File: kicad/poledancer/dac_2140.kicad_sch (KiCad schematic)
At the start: 19 parts, among them U7 AD5328

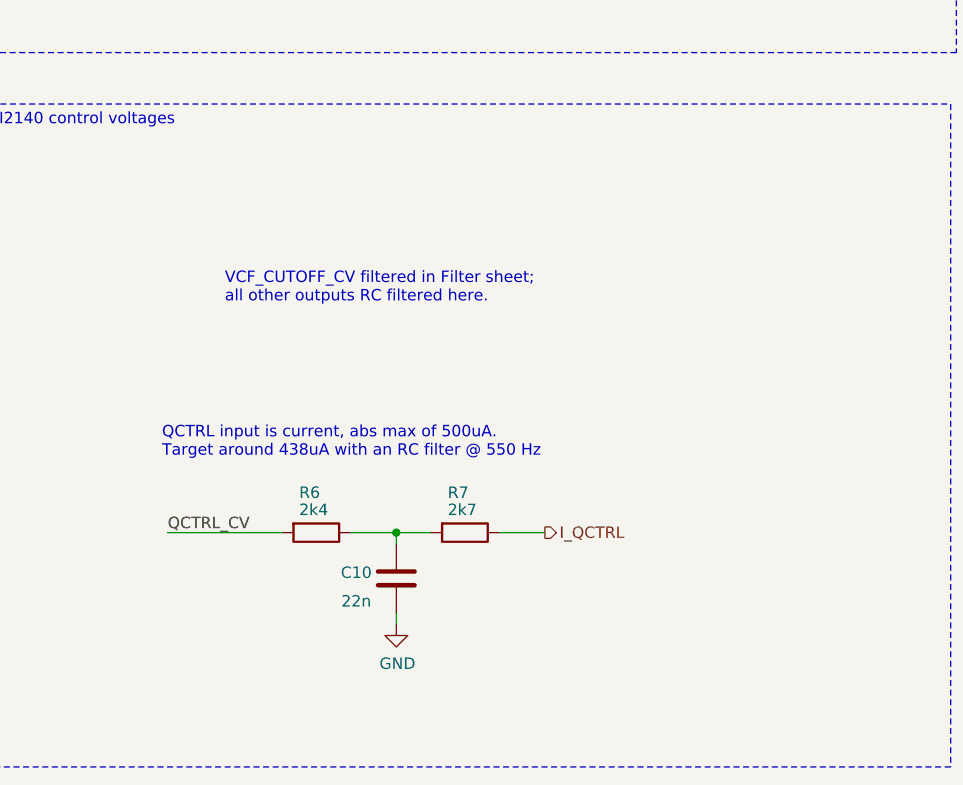
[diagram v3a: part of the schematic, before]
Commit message: create hand solder footprints for SSI chips.  Get some placement done.
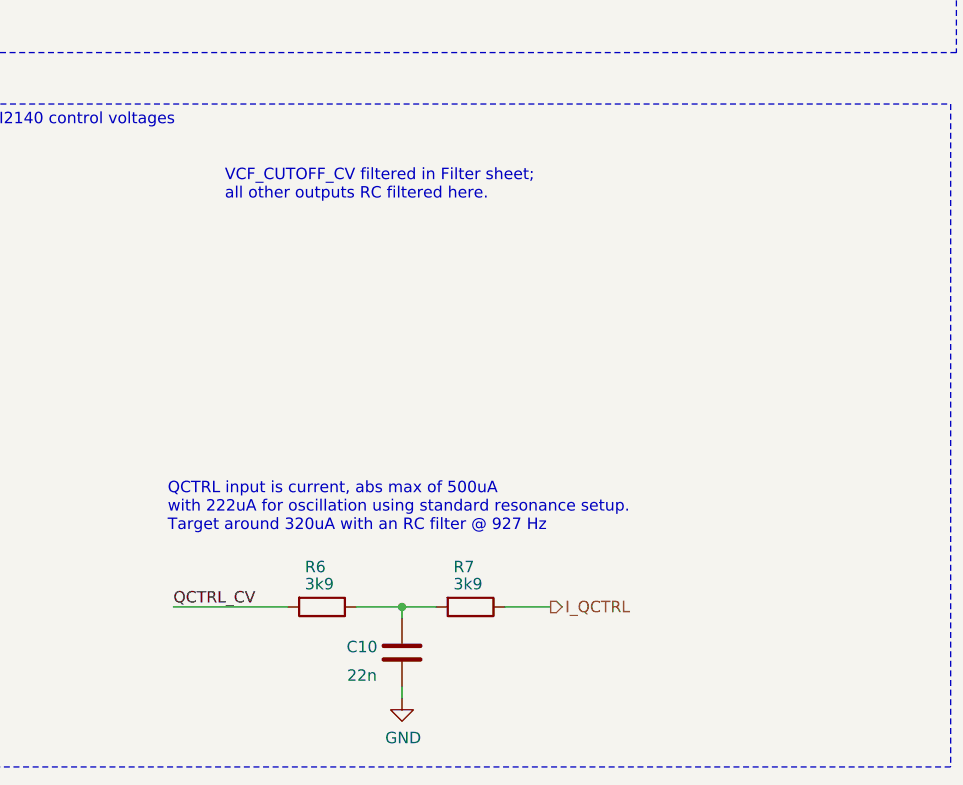
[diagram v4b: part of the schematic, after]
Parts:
- R6: value 2k4 -> 3k9; LCSC C17936 -> C23018
- R7: value 2k7 -> 3k9; LCSC C17936 -> C23018
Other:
- note added: "QCTRL input is current, abs max of 500uA with 222uA for oscillation using standard resonance setup. Target around 320uA with an RC filter @ 927 Hz"
- note removed: "QCTRL input is current, abs max of 500uA. Target around 438uA with an RC filter @ 550 Hz"
- moved on the sheet: C10, R6, R7
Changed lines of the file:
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@@
   (title_block
     (title "Zoxnoxious Pole Dancer Mixing Filter")
-    (date "2022-09-07")
-    (rev "0.4")
+    (date "2024-11-17")
+    (rev "0.1")
     (company "Zoxnoxious Engineering")
   )
@@
   (junction (at 46.99 60.96) (diameter 0) (color 0 0 0 0)
   )
-  (junction (at 71.12 149.86) (diameter 0) (color 0 0 0 0)
+  (junction (at 71.755 158.115) (diameter 0) (color 0 0 0 0)
   )
   (no_connect (at 92.71 68.58))
@@
     (stroke (width 0) (type default))
   )
-  (wire (pts (xy 66.04 149.86) (xy 71.12 149.86))
+  (wire (pts (xy 66.675 158.115) (xy 71.755 158.115))
     (stroke (width 0) (type default))
   )
@@
     (stroke (width 0) (type default))
   )
-  (wire (pts (xy 71.12 158.75) (xy 71.12 160.02))
+  (wire (pts (xy 71.755 167.005) (xy 71.755 168.275))
     (stroke (width 0) (type default))
   )
@@
     (stroke (width 0) (type default))
   )
-  (wire (pts (xy 71.12 149.86) (xy 71.12 151.13))
+  (wire (pts (xy 71.755 158.115) (xy 71.755 159.385))
     (stroke (width 0) (type default))
   )
@@
     (stroke (width 0) (type default))
   )
-  (wire (pts (xy 71.12 149.86) (xy 74.93 149.86))
+  (wire (pts (xy 71.755 158.115) (xy 75.565 158.115))
     (stroke (width 0) (type default))
   )
@@
     (stroke (width 0) (type default))
   )
-  (wire (pts (xy 82.55 149.86) (xy 87.63 149.86))
+  (wire (pts (xy 83.185 158.115) (xy 88.265 158.115))
     (stroke (width 0) (type default))
   )
@@
     (stroke (width 0) (type default))
   )
-  (wire (pts (xy 45.72 149.86) (xy 58.42 149.86))
+  (wire (pts (xy 46.355 158.115) (xy 59.055 158.115))
     (stroke (width 0) (type default))
   )
@@
   )
   (text "VCF_CUTOFF_CV filtered in Filter sheet;\nall other outputs RC filtered here."
-    (at 52.07 124.46 0)
+    (at 52.07 113.03 0)
     (effects (font (size 1.27 1.27)) (justify left bottom))
   )
@@
     (effects (font (size 1.27 1.27)) (justify left bottom))
   )
-  (text "QCTRL input is current, abs max of 500uA.\nTarget around 438uA with an RC filter @ 550 Hz"
-    (at 45.085 141.605 0)
+  (text "QCTRL input is current, abs max of 500uA\nwith 222uA for oscillation using standard resonance setup.\nTarget around 320uA with an RC filter @ 927 Hz"
+    (at 45.72 149.86 0)
     (effects (font (size 1.27 1.27)) (justify left bottom))
   )
@@
     (effects (font (size 1.27 1.27)) (justify left bottom))
   )
-  (label "QCTRL_CV" (at 45.72 149.86 0) (fields_autoplaced)
+  (label "QCTRL_CV" (at 46.355 158.115 0) (fields_autoplaced)
     (effects (font (size 1.27 1.27)) (justify left bottom))
   )
@@
     (effects (font (size 1.27 1.27)) (justify right))
   )
-  (hierarchical_label "I_QCTRL" (shape output) (at 87.63 149.86 0) (fields_autoplaced)
+  (hierarchical_label "I_QCTRL" (shape output) (at 88.265 158.115 0) (fields_autoplaced)
     (effects (font (size 1.27 1.27)) (justify left))
   )
@@
     )
   )
-  (symbol (lib_id "power:GND") (at 71.12 160.02 0) (unit 1)
-    (in_bom yes) (on_board yes) (dnp no)
-    (property "Reference" "#PWR034" (at 71.12 166.37 0)
-      (effects (font (size 1.27 1.27)) hide)
-    )
-    (property "Value" "GND" (at 71.247 164.4142 0)
-      (effects (font (size 1.27 1.27)))
-    )
-    (property "Footprint" "" (at 71.12 160.02 0)
-      (effects (font (size 1.27 1.27)) hide)
-    )
-    (property "Datasheet" "" (at 71.12 160.02 0)
+  (symbol (lib_id "power:GND") (at 71.755 168.275 0) (unit 1)
+    (in_bom yes) (on_board yes) (dnp no)
+    (property "Reference" "#PWR034" (at 71.755 174.625 0)
+      (effects (font (size 1.27 1.27)) hide)
+    )
+    (property "Value" "GND" (at 71.882 172.6692 0)
+      (effects (font (size 1.27 1.27)))
+    )
+    (property "Footprint" "" (at 71.755 168.275 0)
+      (effects (font (size 1.27 1.27)) hide)
+    )
+    (property "Datasheet" "" (at 71.755 168.275 0)
       (effects (font (size 1.27 1.27)) hide)
     )
@@
     )
   )
-  (symbol (lib_id "Device:R") (at 78.74 149.86 270) (unit 1)
-    (in_bom yes) (on_board yes) (dnp no)
-    (property "Reference" "R7" (at 76.835 145.415 90)
-      (effects (font (size 1.27 1.27)) (justify left))
-    )
-    (property "Value" "2k7" (at 76.835 147.32 90)
-      (effects (font (size 1.27 1.27)) (justify left))
-    )
-    (property "Footprint" "Resistor_SMD:R_0603_1608Metric" (at 78.74 148.082 90)
-      (effects (font (size 1.27 1.27)) hide)
-    )
-    (property "Datasheet" "~" (at 78.74 149.86 0)
-      (effects (font (size 1.27 1.27)) hide)
-    )
-    (property "LCSC" "C17936" (at 78.74 149.86 0)
+  (symbol (lib_id "Device:R") (at 79.375 158.115 270) (unit 1)
+    (in_bom yes) (on_board yes) (dnp no)
+    (property "Reference" "R7" (at 77.47 153.67 90)
+      (effects (font (size 1.27 1.27)) (justify left))
+    )
+    (property "Value" "3k9" (at 77.47 155.575 90)
+      (effects (font (size 1.27 1.27)) (justify left))
+    )
+    (property "Footprint" "Resistor_SMD:R_0603_1608Metric" (at 79.375 156.337 90)
+      (effects (font (size 1.27 1.27)) hide)
+    )
+    (property "Datasheet" "~" (at 79.375 158.115 0)
+      (effects (font (size 1.27 1.27)) hide)
+    )
+    (property "LCSC" "C23018" (at 79.375 158.115 0)
       (effects (font (size 1.27 1.27)) hide)
     )
@@
     )
   )
-  (symbol (lib_id "Device:C") (at 71.12 154.94 0) (unit 1)
-    (in_bom yes) (on_board yes) (dnp no)
-    (property "Reference" "C10" (at 66.675 154.305 0)
-      (effects (font (size 1.27 1.27)))
-    )
-    (property "Value" "22n" (at 66.675 157.48 0)
-      (effects (font (size 1.27 1.27)))
-    )
-    (property "Footprint" "Capacitor_SMD:C_0603_1608Metric" (at 72.0852 158.75 0)
-      (effects (font (size 1.27 1.27)) hide)
-    )
-    (property "Datasheet" "~" (at 71.12 154.94 0)
-      (effects (font (size 1.27 1.27)) hide)
-    )
-    (property "LCSC" "C21122" (at 71.12 154.94 0)
+  (symbol (lib_id "Device:C") (at 71.755 163.195 0) (unit 1)
+    (in_bom yes) (on_board yes) (dnp no)
+    (property "Reference" "C10" (at 67.31 162.56 0)
+      (effects (font (size 1.27 1.27)))
+    )
+    (property "Value" "22n" (at 67.31 165.735 0)
+      (effects (font (size 1.27 1.27)))
+    )
+    (property "Footprint" "Capacitor_SMD:C_0603_1608Metric" (at 72.7202 167.005 0)
+      (effects (font (size 1.27 1.27)) hide)
+    )
+    (property "Datasheet" "~" (at 71.755 163.195 0)
+      (effects (font (size 1.27 1.27)) hide)
+    )
+    (property "LCSC" "C21122" (at 71.755 163.195 0)
       (effects (font (size 1.27 1.27)) hide)
     )
@@
     )
   )
-  (symbol (lib_id "Device:R") (at 62.23 149.86 270) (unit 1)
-    (in_bom yes) (on_board yes) (dnp no)
-    (property "Reference" "R6" (at 60.325 145.415 90)
-      (effects (font (size 1.27 1.27)) (justify left))
-    )
-    (property "Value" "2k4" (at 60.325 147.32 90)
-      (effects (font (size 1.27 1.27)) (justify left))
-    )
-    (property "Footprint" "Resistor_SMD:R_0603_1608Metric" (at 62.23 148.082 90)
-      (effects (font (size 1.27 1.27)) hide)
-    )
-    (property "Datasheet" "~" (at 62.23 149.86 0)
-      (effects (font (size 1.27 1.27)) hide)
-    )
-    (property "LCSC" "C17936" (at 62.23 149.86 0)
-      (effects (font (size 1.27 1.27)) hide)
-    )
+  (symbol (lib_id "Device:R") (at 62.865 158.115 270) (unit 1)
+    (in_bom yes) (on_board yes) (dnp no)
+    (property "Reference" "R6" (at 60.96 153.67 90)
+      (effects (font (size 1.27 1.27)) (justify left))
+    )
+    (property "Value" "3k9" (at 60.96 155.575 90)
+      (effects (font (size 1.27 1.27)) (justify left))
+    )
+    (property "Footprint" "Resistor_SMD:R_0603_1608Metric" (at 62.865 156.337 90)
+      (effects (font (size 1.27 1.27)) hide)
+    )
+    (property "Datasheet" "~" (at 62.865 158.115 0)
+      (effects (font (size 1.27 1.27)) hide)
+    )
+    (property "LCSC" "C23018" (at 62.865 158.115 0)
+      (effects (font (size 1.27 1.27)) hide)
+    )

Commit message: updated rez comp mode.  Back to placement on PCB.
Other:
- note added: "Sheet Vref load: 45k || 45k ==> 22.5k"
- note removed: "LM4040 resistor rough calc: Ilm4040 min: 70uA"
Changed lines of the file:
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@@
     (effects (font (size 1.27 1.27)) (justify left bottom))
   )
-  (text "LM4040 resistor rough calc:\nIlm4040 min:  70uA\n" (at 40.64 88.9 0)
+  (text "Sheet Vref load: 45k || 45k ==> 22.5k" (at 260.985 23.495 0)
     (effects (font (size 1.27 1.27)) (justify left bottom))
   )

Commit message: continue placement
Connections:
- net SOURCE2_MOD: now also U7.13 (VOUT_H); no longer U7.12 (VOUT_G)
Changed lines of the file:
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@@
   (junction (at 71.755 158.115) (diameter 0) (color 0 0 0 0)
   )
-  (no_connect (at 92.71 68.58))
+  (no_connect (at 92.71 66.04))
   (no_connect (at 92.71 55.88))
   (wire (pts (xy 214.63 45.72) (xy 219.71 45.72))
@@
     (stroke (width 0) (type default))
   )
-  (wire (pts (xy 92.71 66.04) (xy 110.49 66.04))
+  (wire (pts (xy 92.71 68.58) (xy 110.49 68.58))
     (stroke (width 0) (type default))
   )
@@
     (effects (font (size 1.27 1.27)) (justify right bottom))
   )
-  (label "SOURCE2_MOD" (at 110.49 66.04 180) (fields_autoplaced)
+  (label "SOURCE2_MOD" (at 110.49 68.58 180) (fields_autoplaced)
     (effects (font (size 1.27 1.27)) (justify right bottom))
   )

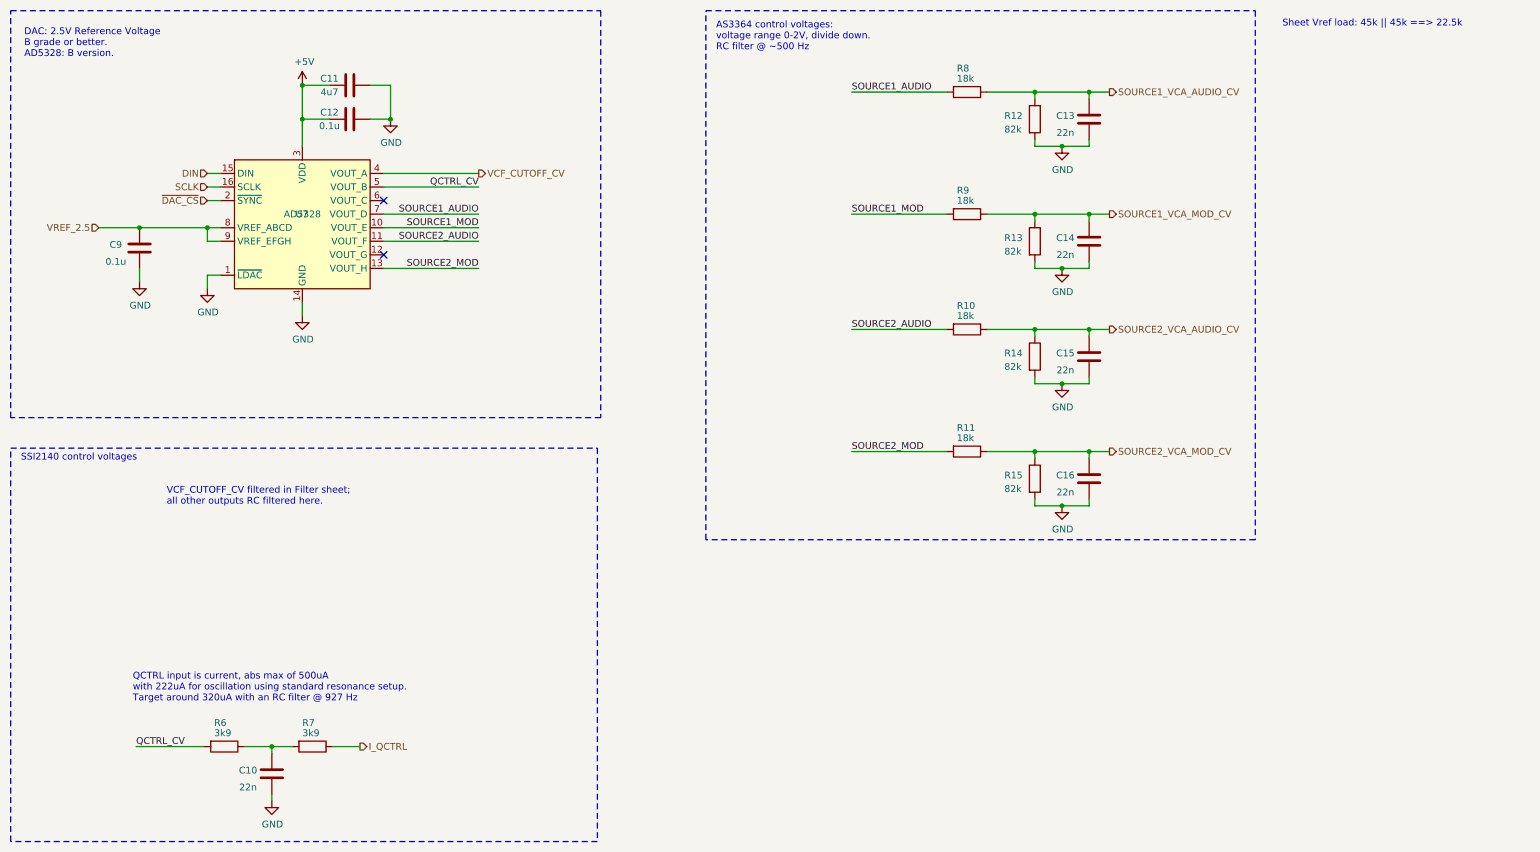
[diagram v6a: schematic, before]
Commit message: start routing power
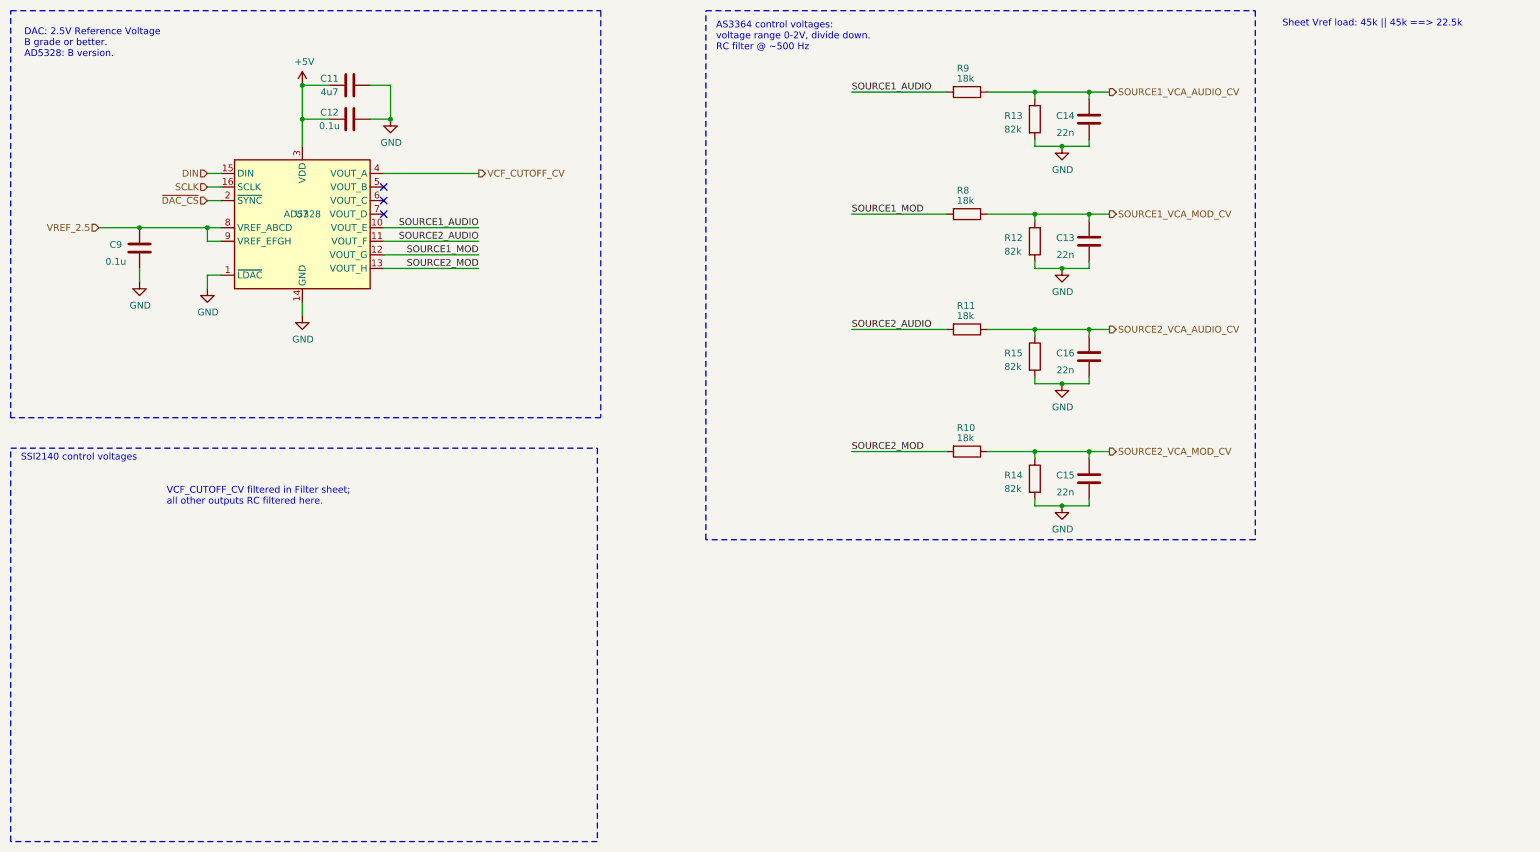
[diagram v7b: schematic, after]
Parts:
- removed C10: 22n, Capacitor_SMD:C_0603_1608Metric, symbol Device:C
- removed R6, R7: 3k9, Resistor_SMD:R_0603_1608Metric, symbol Device:R
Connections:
- net SOURCE1_AUDIO: now also R9.2, U7.10 (VOUT_E); no longer R8.2, U7.7 (VOUT_D)
- net SOURCE1_MOD: now also R8.2, U7.12 (VOUT_G); no longer R9.2, U7.10 (VOUT_E)
- net SOURCE1_VCA_AUDIO_CV: now also C14.1, R13.1, R9.1; no longer C13.1, R12.1, R8.1
- net SOURCE1_VCA_MOD_CV: now also C13.1, R12.1, R8.1; no longer C14.1, R13.1, R9.1
- net SOURCE2_AUDIO: now also R11.2; no longer R10.2
- net SOURCE2_MOD: now also R10.2; no longer R11.2
- net SOURCE2_VCA_AUDIO_CV: now also C16.1, R11.1, R15.1; no longer C15.1, R10.1, R14.1
- net SOURCE2_VCA_MOD_CV: now also C15.1, R10.1, R14.1; no longer C16.1, R11.1, R15.1
- net QCTRL_CV: no longer names the net of U7.5 (VOUT_B)
- no-connect marks 2 -> 3
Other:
- note removed: "QCTRL input is current, abs max of 500uA with 222uA for oscillation using standard resonance setup. Target around 320uA with an RC filter @ 927 Hz"
- moved on the sheet: C13, C14, C15, C16, R10, R11, R12, R13, R14, R15, R8, R9
